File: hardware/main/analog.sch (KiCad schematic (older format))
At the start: 45 parts, among them U2 LM324, U301 LM324

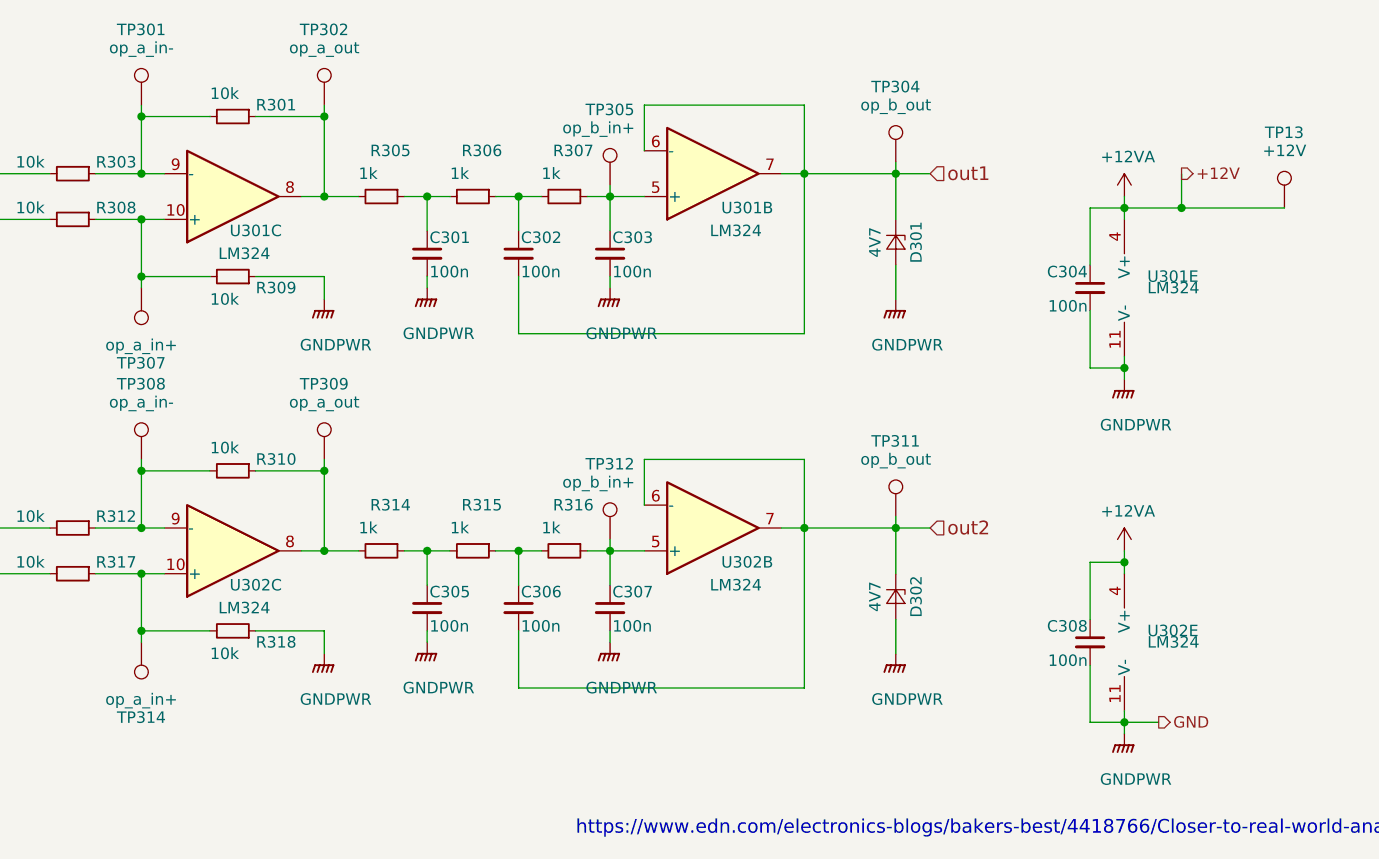
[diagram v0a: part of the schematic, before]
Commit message: Copper bar fixation
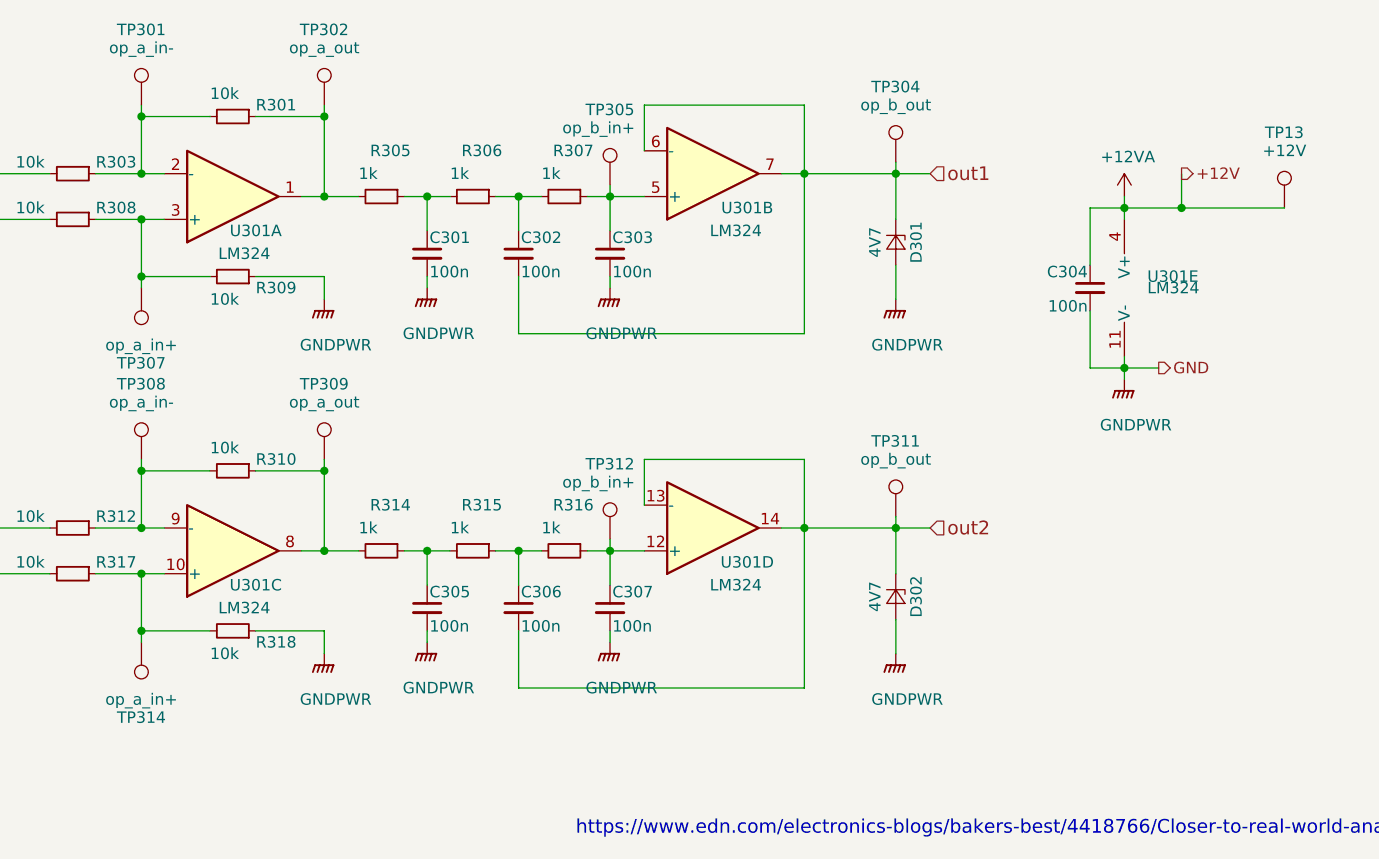
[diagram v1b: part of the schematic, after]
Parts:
- removed C11: 100n, Capacitor_SMD:C_0805_2012Metric_Pad1.15x1.40mm_HandSolder, symbol Device:C_Small
- removed unit 5 of U2
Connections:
- net out2: now also U2.13 (-), U2.14; no longer U2.6 (-), U2.7
- net at R301.2, R303.1, TP301.1: now also U301.2 (-); no longer U301.9 (-)
- net at R308.1, R309.2, TP307.1: now also U301.3 (+); no longer U301.10 (+)
- net at R301.1, R305.2, TP302.1: now also U301.1; no longer U301.8
- net at C9.1, R31.1, TP12.1: now also U2.12 (+); no longer U2.5 (+)
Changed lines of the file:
@@
 $Descr A4 11693 8268
 encoding utf-8
-Sheet 3 8
+Sheet 3 9
 Title ""
 Date ""
@@
 $Comp
 L Amplifier_Operational:LM324 U301
-U 3 1 5BE784E0
+U 1 1 5BE784E0
 P 4950 3650
 AR Path="/5BE784E0" Ref="U301"  Part="3"
@@
 AR Path="/5C9FC045/5BE784E0" Ref="U1"  Part="3"
 AR Path="/5CA4DC1F/5CA5A61A/5BE784E0" Ref="U901"  Part="3"
-AR Path="/5C9C4D6B/5CBAEDA0/5BE784E0" Ref="U301"  Part="3"
+AR Path="/5C9C4D6B/5CBAEDA0/5BE784E0" Ref="U301"  Part="1"
 AR Path="/5CBD2CE3/5CBAEDA0/5BE784E0" Ref="U?"  Part="3"
 F 0 "U301" H 5050 3800 50  0000 C CNN
@@
 F 2 "Package_SO:SOIC-14_3.9x8.7mm_P1.27mm" H 4900 3750 50  0001 C CNN
 F 3 "http://www.ti.com/lit/ds/symlink/lm2902-n.pdf" H 5000 3850 50  0001 C CNN
-	3    4950 3650
+	1    4950 3650
 	1    0    0    1
 $EndComp
@@
 AR Path="/5C9FC045/5CA04791" Ref="U2"  Part="3"
 AR Path="/5CA4DC1F/5CA5A61A/5CA04791" Ref="U902"  Part="3"
-AR Path="/5C9C4D6B/5CBAEDA0/5CA04791" Ref="U302"  Part="3"
+AR Path="/5C9C4D6B/5CBAEDA0/5CA04791" Ref="U301"  Part="3"
 AR Path="/5CBD2CE3/5CBAEDA0/5CA04791" Ref="U?"  Part="3"
-F 0 "U302" H 5050 5350 50  0000 C CNN
+F 0 "U301" H 5050 5350 50  0000 C CNN
 F 1 "LM324" H 5000 5450 50  0000 C CNN
 F 2 "Package_SO:SOIC-14_3.9x8.7mm_P1.27mm" H 4900 5300 50  0001 C CNN
@@
 $Comp
 L Amplifier_Operational:LM324 U?
-U 2 1 5CA04797
+U 4 1 5CA04797
 P 7050 5100
 AR Path="/5CA04797" Ref="U?"  Part="2"
@@
 AR Path="/5C9FC045/5CA04797" Ref="U2"  Part="2"
 AR Path="/5CA4DC1F/5CA5A61A/5CA04797" Ref="U902"  Part="2"
-AR Path="/5C9C4D6B/5CBAEDA0/5CA04797" Ref="U302"  Part="2"
+AR Path="/5C9C4D6B/5CBAEDA0/5CA04797" Ref="U301"  Part="4"
 AR Path="/5CBD2CE3/5CBAEDA0/5CA04797" Ref="U?"  Part="2"
-F 0 "U302" H 7200 5250 50  0000 C CNN
+F 0 "U301" H 7200 5250 50  0000 C CNN
 F 1 "LM324" H 7150 5350 50  0000 C CNN
 F 2 "Package_SO:SOIC-14_3.9x8.7mm_P1.27mm" H 7000 5200 50  0001 C CNN
 F 3 "http://www.ti.com/lit/ds/symlink/lm2902-n.pdf" H 7100 5300 50  0001 C CNN
-	2    7050 5100
+	4    7050 5100
 	1    0    0    1
 $EndComp
-$Comp
-L Amplifier_Operational:LM324 U?
-U 5 1 5CA0479D
-P 8750 5600
-AR Path="/5CA0479D" Ref="U?"  Part="5"
-AR Path="/5AAC947C/5CA0479D" Ref="U?"  Part="5"
-AR Path="/5C9FC045/5CA0479D" Ref="U2"  Part="5"
-AR Path="/5CA4DC1F/5CA5A61A/5CA0479D" Ref="U902"  Part="5"
-AR Path="/5C9C4D6B/5CBAEDA0/5CA0479D" Ref="U302"  Part="5"
-AR Path="/5CBD2CE3/5CBAEDA0/5CA0479D" Ref="U?"  Part="5"
-F 0 "U302" H 8550 5650 50  0000 R CNN
-F 1 "LM324" H 8550 5600 50  0000 R CNN
-F 2 "Package_SO:SOIC-14_3.9x8.7mm_P1.27mm" H 8700 5700 50  0001 C CNN
-F 3 "http://www.ti.com/lit/ds/symlink/lm2902-n.pdf" H 8800 5800 50  0001 C CNN
-	5    8750 5600
-	-1   0    0    -1
-$EndComp
-$Comp
-L Device:C_Small C?
-U 1 1 5CA047A3
-P 8700 5600
-AR Path="/5CA047A3" Ref="C?"  Part="1"
-AR Path="/5AAC947C/5CA047A3" Ref="C?"  Part="1"
-AR Path="/5C9FC045/5CA047A3" Ref="C11"  Part="1"
-AR Path="/5CA4DC1F/5CA5A61A/5CA047A3" Ref="C908"  Part="1"
-AR Path="/5C9C4D6B/5CBAEDA0/5CA047A3" Ref="C308"  Part="1"
-AR Path="/5CBD2CE3/5CBAEDA0/5CA047A3" Ref="C?"  Part="1"
-F 0 "C308" H 8710 5670 50  0000 L CNN
-F 1 "100n" H 8710 5520 50  0000 L CNN
-F 2 "Capacitor_SMD:C_0805_2012Metric_Pad1.15x1.40mm_HandSolder" H 8700 5600 50  0001 C CNN
-F 3 "" H 8700 5600 50  0001 C CNN
-	1    8700 5600
-	-1   0    0    -1
-$EndComp
-Wire Wire Line
-	8850 5950 8700 5950
-Wire Wire Line
-	8700 5950 8700 5700
-Wire Wire Line
-	8850 5900 8850 5950
-Connection ~ 8850 5950
-Wire Wire Line
-	8850 5950 8850 6000
-Wire Wire Line
-	8850 5250 8700 5250
-Wire Wire Line
-	8700 5250 8700 5500
-Wire Wire Line
-	8850 5200 8850 5250
-Connection ~ 8850 5250
-Wire Wire Line
-	8850 5250 8850 5300
 Wire Wire Line
 	4550 5550 4850 5550
@@
 $EndComp
 $Comp
-L power:GNDPWR #PWR0113
-U 1 1 5CBE982F
-P 8850 6000
-F 0 "#PWR0113" H 8850 5800 50  0001 C CNN
-F 1 "GNDPWR" H 8900 5800 50  0000 C CNN
-F 2 "" H 8850 5950 50  0001 C CNN
-F 3 "" H 8850 5950 50  0001 C CNN
-	1    8850 6000
-	1    0    0    -1
-$EndComp
-$Comp
 L power:GNDPWR #PWR0114
 U 1 1 5CBE9DBF
@@
 F 3 "" H 8850 3650 50  0001 C CNN
 	1    8850 3650
-	1    0    0    -1
-$EndComp
-$Comp
-L power:+12VA #PWR0148
-U 1 1 5CA79715
-P 8850 5200
-F 0 "#PWR0148" H 8850 5050 50  0001 C CNN
-F 1 "+12VA" H 8865 5373 50  0000 C CNN
-F 2 "" H 8850 5200 50  0001 C CNN
-F 3 "" H 8850 5200 50  0001 C CNN
-	1    8850 5200
 	1    0    0    -1
 $EndComp
@@
 	9100 3700 9550 3700
 Connection ~ 9100 3700
-Text HLabel 9000 5950 2    50   Output ~ 0
+Text HLabel 9000 4400 2    50   Output ~ 0
 GND
 Wire Wire Line
-	8850 5950 9000 5950
+	9000 4400 8850 4400
 $EndSCHEMATC

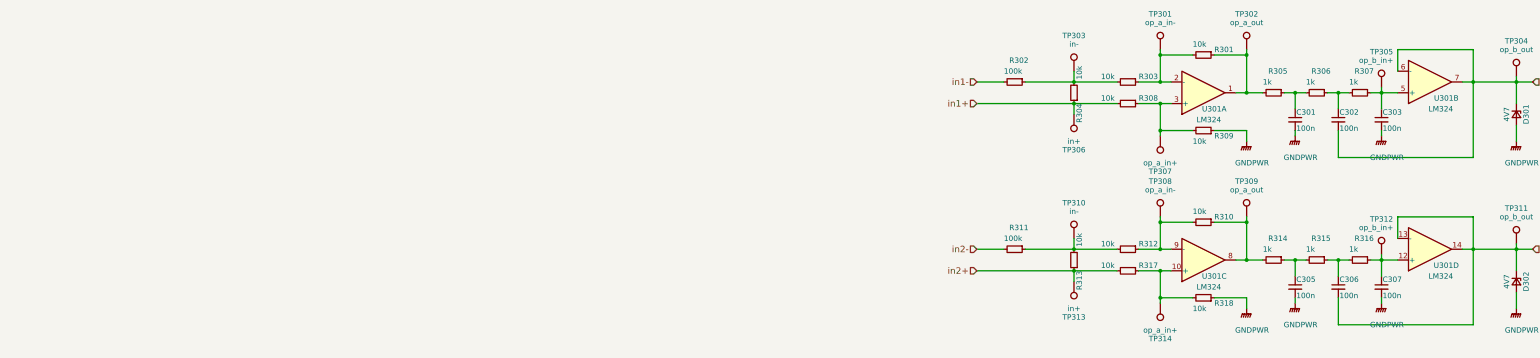
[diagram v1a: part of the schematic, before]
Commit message: Ampop layout not finished
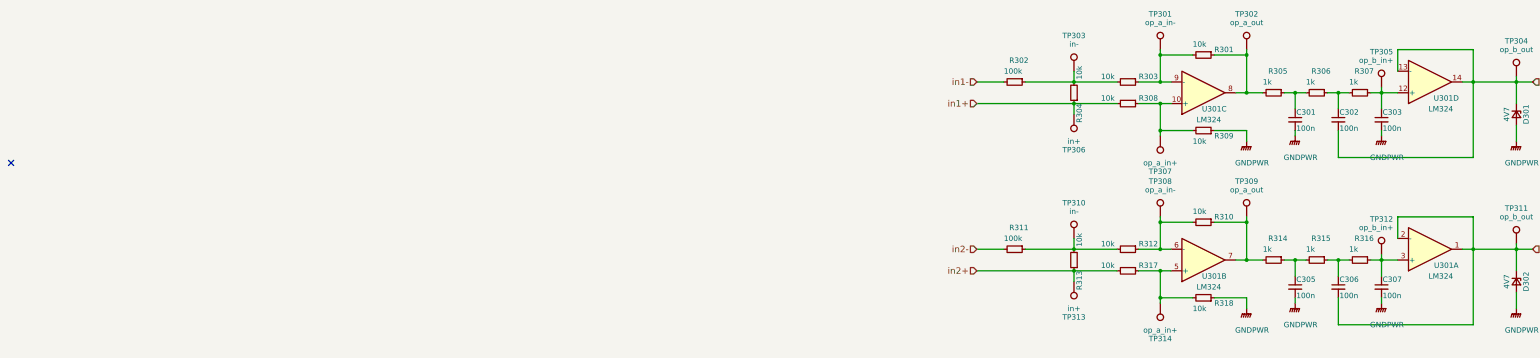
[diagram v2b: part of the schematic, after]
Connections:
- net out1: now also U301.13 (-), U301.14; no longer U301.6 (-), U301.7
- net out2: now also U2.1, U2.2 (-); no longer U2.13 (-), U2.14
- net at R301.2, R303.1, TP301.1: now also U301.9 (-); no longer U301.2 (-)
- net at R308.1, R309.2, TP307.1: now also U301.10 (+); no longer U301.3 (+)
- net at C303.1, R307.1, TP305.1: now also U301.12 (+); no longer U301.5 (+)
- net at R301.1, R305.2, TP302.1: now also U301.8; no longer U301.1
- net at R20.1, R24.2, TP7.1: now also U2.6 (-); no longer U2.9 (-)
- net at R21.1, R25.2, TP8.1: now also U2.5 (+); no longer U2.10 (+)
- net at C9.1, R31.1, TP12.1: now also U2.3 (+); no longer U2.12 (+)
- net at R24.1, R27.2, TP10.1: now also U2.7; no longer U2.8
- no-connect marks 0 -> 1
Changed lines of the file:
@@
 $Comp
 L Amplifier_Operational:LM324 U301
-U 1 1 5BE784E0
+U 3 1 5BE784E0
 P 4950 3650
 AR Path="/5BE784E0" Ref="U301"  Part="3"
@@
 AR Path="/5C9FC045/5BE784E0" Ref="U1"  Part="3"
 AR Path="/5CA4DC1F/5CA5A61A/5BE784E0" Ref="U901"  Part="3"
-AR Path="/5C9C4D6B/5CBAEDA0/5BE784E0" Ref="U301"  Part="1"
+AR Path="/5C9C4D6B/5CBAEDA0/5BE784E0" Ref="U301"  Part="3"
 AR Path="/5CBD2CE3/5CBAEDA0/5BE784E0" Ref="U?"  Part="3"
 F 0 "U301" H 5050 3800 50  0000 C CNN
@@
 F 2 "Package_SO:SOIC-14_3.9x8.7mm_P1.27mm" H 4900 3750 50  0001 C CNN
 F 3 "http://www.ti.com/lit/ds/symlink/lm2902-n.pdf" H 5000 3850 50  0001 C CNN
-	1    4950 3650
+	3    4950 3650
 	1    0    0    1
 $EndComp
 $Comp
 L Amplifier_Operational:LM324 U301
-U 2 1 5BE7C0AB
+U 4 1 5BE7C0AB
 P 7050 3550
 AR Path="/5BE7C0AB" Ref="U301"  Part="2"
@@
 AR Path="/5C9FC045/5BE7C0AB" Ref="U1"  Part="2"
 AR Path="/5CA4DC1F/5CA5A61A/5BE7C0AB" Ref="U901"  Part="2"
-AR Path="/5C9C4D6B/5CBAEDA0/5BE7C0AB" Ref="U301"  Part="2"
+AR Path="/5C9C4D6B/5CBAEDA0/5BE7C0AB" Ref="U301"  Part="4"
 AR Path="/5CBD2CE3/5CBAEDA0/5BE7C0AB" Ref="U?"  Part="2"
 F 0 "U301" H 7200 3700 50  0000 C CNN
@@
 F 2 "Package_SO:SOIC-14_3.9x8.7mm_P1.27mm" H 7000 3650 50  0001 C CNN
 F 3 "http://www.ti.com/lit/ds/symlink/lm2902-n.pdf" H 7100 3750 50  0001 C CNN
-	2    7050 3550
+	4    7050 3550
 	1    0    0    1
 $EndComp
@@
 $Comp
 L Amplifier_Operational:LM324 U?
-U 3 1 5CA04791
+U 2 1 5CA04791
 P 4950 5200
 AR Path="/5CA04791" Ref="U?"  Part="3"
@@
 AR Path="/5C9FC045/5CA04791" Ref="U2"  Part="3"
 AR Path="/5CA4DC1F/5CA5A61A/5CA04791" Ref="U902"  Part="3"
-AR Path="/5C9C4D6B/5CBAEDA0/5CA04791" Ref="U301"  Part="3"
+AR Path="/5C9C4D6B/5CBAEDA0/5CA04791" Ref="U301"  Part="2"
 AR Path="/5CBD2CE3/5CBAEDA0/5CA04791" Ref="U?"  Part="3"
 F 0 "U301" H 5050 5350 50  0000 C CNN
@@
 F 2 "Package_SO:SOIC-14_3.9x8.7mm_P1.27mm" H 4900 5300 50  0001 C CNN
 F 3 "http://www.ti.com/lit/ds/symlink/lm2902-n.pdf" H 5000 5400 50  0001 C CNN
-	3    4950 5200
+	2    4950 5200
 	1    0    0    1
 $EndComp
 $Comp
 L Amplifier_Operational:LM324 U?
-U 4 1 5CA04797
+U 1 1 5CA04797
 P 7050 5100
 AR Path="/5CA04797" Ref="U?"  Part="2"
@@
 AR Path="/5C9FC045/5CA04797" Ref="U2"  Part="2"
 AR Path="/5CA4DC1F/5CA5A61A/5CA04797" Ref="U902"  Part="2"
-AR Path="/5C9C4D6B/5CBAEDA0/5CA04797" Ref="U301"  Part="4"
+AR Path="/5C9C4D6B/5CBAEDA0/5CA04797" Ref="U301"  Part="1"
 AR Path="/5CBD2CE3/5CBAEDA0/5CA04797" Ref="U?"  Part="2"
 F 0 "U301" H 7200 5250 50  0000 C CNN
@@
 F 2 "Package_SO:SOIC-14_3.9x8.7mm_P1.27mm" H 7000 5200 50  0001 C CNN
 F 3 "http://www.ti.com/lit/ds/symlink/lm2902-n.pdf" H 7100 5300 50  0001 C CNN
-	4    7050 5100
+	1    7050 5100
 	1    0    0    1
 $EndComp
@@
 $EndComp
 $Comp
-L power:GNDPWR #PWR0142
-U 1 1 5CBEAA58
-P 5350 4100
-F 0 "#PWR0142" H 5350 3900 50  0001 C CNN
-F 1 "GNDPWR" H 5400 3900 50  0000 C CNN
-F 2 "" H 5350 4050 50  0001 C CNN
-F 3 "" H 5350 4050 50  0001 C CNN
-	1    5350 4100
-	1    0    0    -1
-$EndComp
-$Comp
 L power:GNDPWR #PWR0143
 U 1 1 5CBEACE6
@@
 Wire Wire Line
 	9000 4400 8850 4400
+$Comp
+L power:GNDPWR #PWR0142
+U 1 1 5CBEAA58
+P 5350 4100
+F 0 "#PWR0142" H 5350 3900 50  0001 C CNN
+F 1 "GNDPWR" H 5400 3900 50  0000 C CNN
+F 2 "" H 5350 4050 50  0001 C CNN
+F 3 "" H 5350 4050 50  0001 C CNN
+	1    5350 4100
+	1    0    0    -1
+$EndComp
+NoConn ~ -6100 4300
 $EndSCHEMATC

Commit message: Circuito ampop incompleto
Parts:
- TP10, TP12, TP13, TP14, TP3, TP301, TP302, TP303, TP304, TP305, TP306, TP307, TP4, TP7, TP8: footprint TestPoint:TestPoint_Pad_2.0x2.0mm -> TestPoint:TestPoint_Pad_D1.5mm
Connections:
- net out1: now also U301.8, U301.9 (-); no longer U301.13 (-), U301.14
- net out2: now also U2.13 (-), U2.14; no longer U2.1, U2.2 (-)
- net at R301.2, R303.1, TP301.1: now also U301.6 (-); no longer U301.9 (-)
- net at R308.1, R309.2, TP307.1: now also U301.5 (+); no longer U301.10 (+)
- net at C303.1, R307.1, TP305.1: now also U301.10 (+); no longer U301.12 (+)
- net at R301.1, R305.2, TP302.1: now also U301.7; no longer U301.8
- net at R20.1, R24.2, TP7.1: now also U2.2 (-); no longer U2.6 (-)
- net at R21.1, R25.2, TP8.1: now also U2.3 (+); no longer U2.5 (+)
- net at C9.1, R31.1, TP12.1: now also U2.12 (+); no longer U2.3 (+)
- net at R24.1, R27.2, TP10.1: now also U2.1; no longer U2.7

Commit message: First version PCB
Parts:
- removed TP10, TP302: op_a_out, TestPoint:TestPoint_Pad_D1.5mm, symbol Connector:TestPoint
- removed TP12, TP305: op_b_in+, TestPoint:TestPoint_Pad_D1.5mm, symbol Connector:TestPoint
- removed TP13: +12V, TestPoint:TestPoint_Pad_D1.5mm, symbol Connector:TestPoint
- removed TP14, TP304: op_b_out, TestPoint:TestPoint_Pad_D1.5mm, symbol Connector:TestPoint
- removed TP3, TP303: in-, TestPoint:TestPoint_Pad_D1.5mm, symbol Connector:TestPoint
- removed TP301, TP7: op_a_in-, TestPoint:TestPoint_Pad_D1.5mm, symbol Connector:TestPoint
- removed TP306, TP4: in+, TestPoint:TestPoint_Pad_D1.5mm, symbol Connector:TestPoint
- removed TP307, TP8: op_a_in+, TestPoint:TestPoint_Pad_D1.5mm, symbol Connector:TestPoint
